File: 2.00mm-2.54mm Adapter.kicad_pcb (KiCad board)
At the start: 2 copper layers, 23.5 x 53 mm, 4 parts, among them J101 Conn_02x20_Odd_Even, J102 Conn_02x20_Odd_Even

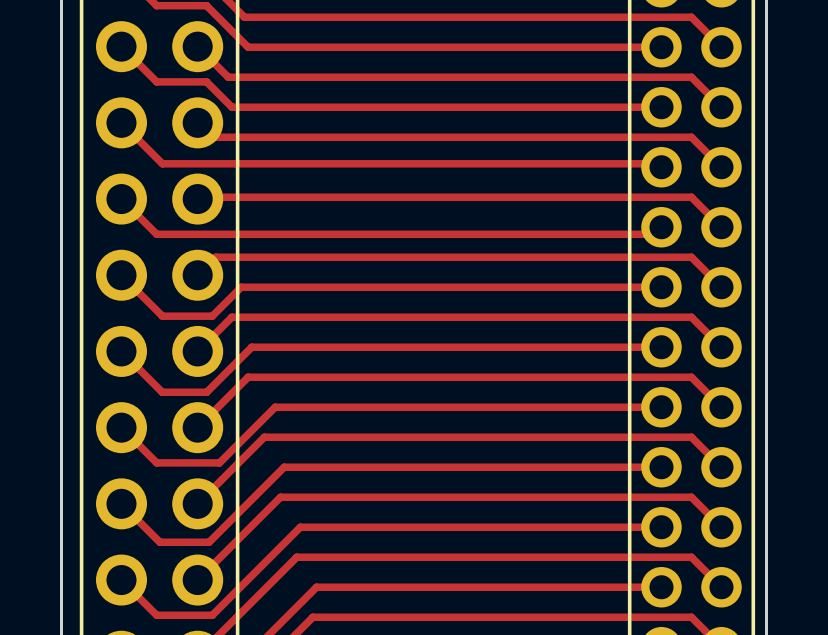
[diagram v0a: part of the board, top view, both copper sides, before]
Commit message: Added silkscreen
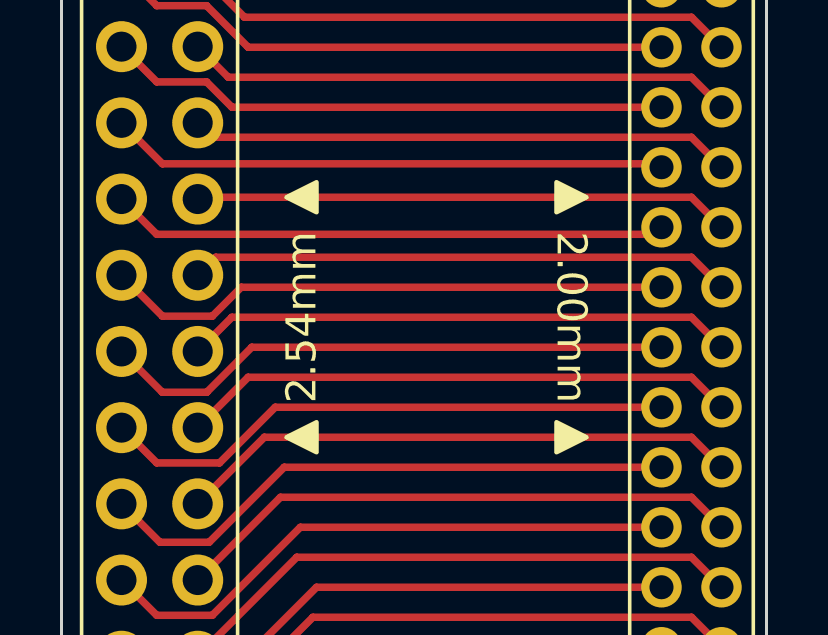
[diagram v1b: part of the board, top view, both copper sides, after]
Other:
- board text added: "2.00mm"
- board text added: "2.54mm"
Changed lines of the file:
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@@
     )
   )
+  (gr_poly
+    (pts
+      (xy 127.5 99.5)
+      (xy 126.5 100)
+      (xy 127.5 100.5)
+    )
+    (stroke (width 0.15) (type solid)) (fill solid) (layer "F.SilkS"))
+  (gr_poly
+    (pts
+      (xy 135.5 92.5)
+      (xy 136.5 92)
+      (xy 135.5 91.5)
+    )
+    (stroke (width 0.15) (type solid)) (fill solid) (layer "F.SilkS"))
+  (gr_poly
+    (pts
+      (xy 135.5 100.5)
+      (xy 136.5 100)
+      (xy 135.5 99.5)
+    )
+    (stroke (width 0.15) (type solid)) (fill solid) (layer "F.SilkS"))
+  (gr_poly
+    (pts
+      (xy 127.5 91.5)
+      (xy 126.5 92)
+      (xy 127.5 92.5)
+    )
+    (stroke (width 0.15) (type solid)) (fill solid) (layer "F.SilkS"))
   (gr_arc (start 141.5 69.5) (mid 142.207107 69.792893) (end 142.5 70.5)
     (stroke (width 0.1) (type default)) (layer "Edge.Cuts"))
@@
   (gr_line (start 119 70.5) (end 119 121.5)
     (stroke (width 0.1) (type default)) (layer "Edge.Cuts"))
+  (gr_text "2.54mm" (at 127 96 90) (layer "F.SilkS")
+    (effects (font (size 1 1) (thickness 0.15)))
+  )
+  (gr_text "2.00mm" (at 136 96 270) (layer "F.SilkS")
+    (effects (font (size 1 1) (thickness 0.15)))
+  )
+  (dimension (type aligned) (layer "Cmts.User")
+    (pts (xy 119 69.5) (xy 119 122.5))
+    (height 2)
+    (gr_text "53.0000 mm" (at 115.85 96 90) (layer "Cmts.User")
+      (effects (font (size 1 1) (thickness 0.15)))
+    )
+    (format (prefix "") (suffix "") (units 3) (units_format 1) (precision 4))
+    (style (thickness 0.15) (arrow_length 1.27) (text_position_mode 0) (extension_height 0.58642) (extension_offset 0.5) keep_text_aligned)
+  )
+  (dimension (type aligned) (layer "Cmts.User")
+    (pts (xy 142.5 69.5) (xy 119 69.5))
+    (height 2)
+    (gr_text "23.5000 mm" (at 130.75 66.35) (layer "Cmts.User")
+      (effects (font (size 1 1) (thickness 0.15)))
+    )
+    (format (prefix "") (suffix "") (units 3) (units_format 1) (precision 4))
+    (style (thickness 0.15) (arrow_length 1.27) (text_position_mode 0) (extension_height 0.58642) (extension_offset 0.5) keep_text_aligned)
+  )
+  (dimension (type aligned) (layer "Cmts.User")
+    (pts (xy 129.5 69.5) (xy 129.5 96))
+    (height -2.5)
+    (gr_text "26.5000 mm" (at 130.85 82.75 90) (layer "Cmts.User")
+      (effects (font (size 1 1) (thickness 0.15)))
+    )
+    (format (prefix "") (suffix "") (units 3) (units_format 1) (precision 4))
+    (style (thickness 0.15) (arrow_length 1.27) (text_position_mode 0) (extension_height 0.58642) (extension_offset 0.5) keep_text_aligned)
+  )
   (segment (start 122.365 73.105) (end 121 71.74) (width 0.25) (layer "F.Cu") (net 1))
   (segment (start 139 77) (end 135.105 73.105) (width 0.25) (layer "F.Cu") (net 1))
